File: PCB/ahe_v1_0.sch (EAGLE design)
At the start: 19 parts, among them IC1 MS560702BA03-50, IC2 MCP73871-1CCI_ML, IC3 ESP32-S2-WROOM-I_M22S2H3200UH3, J1 USB3075-30-A

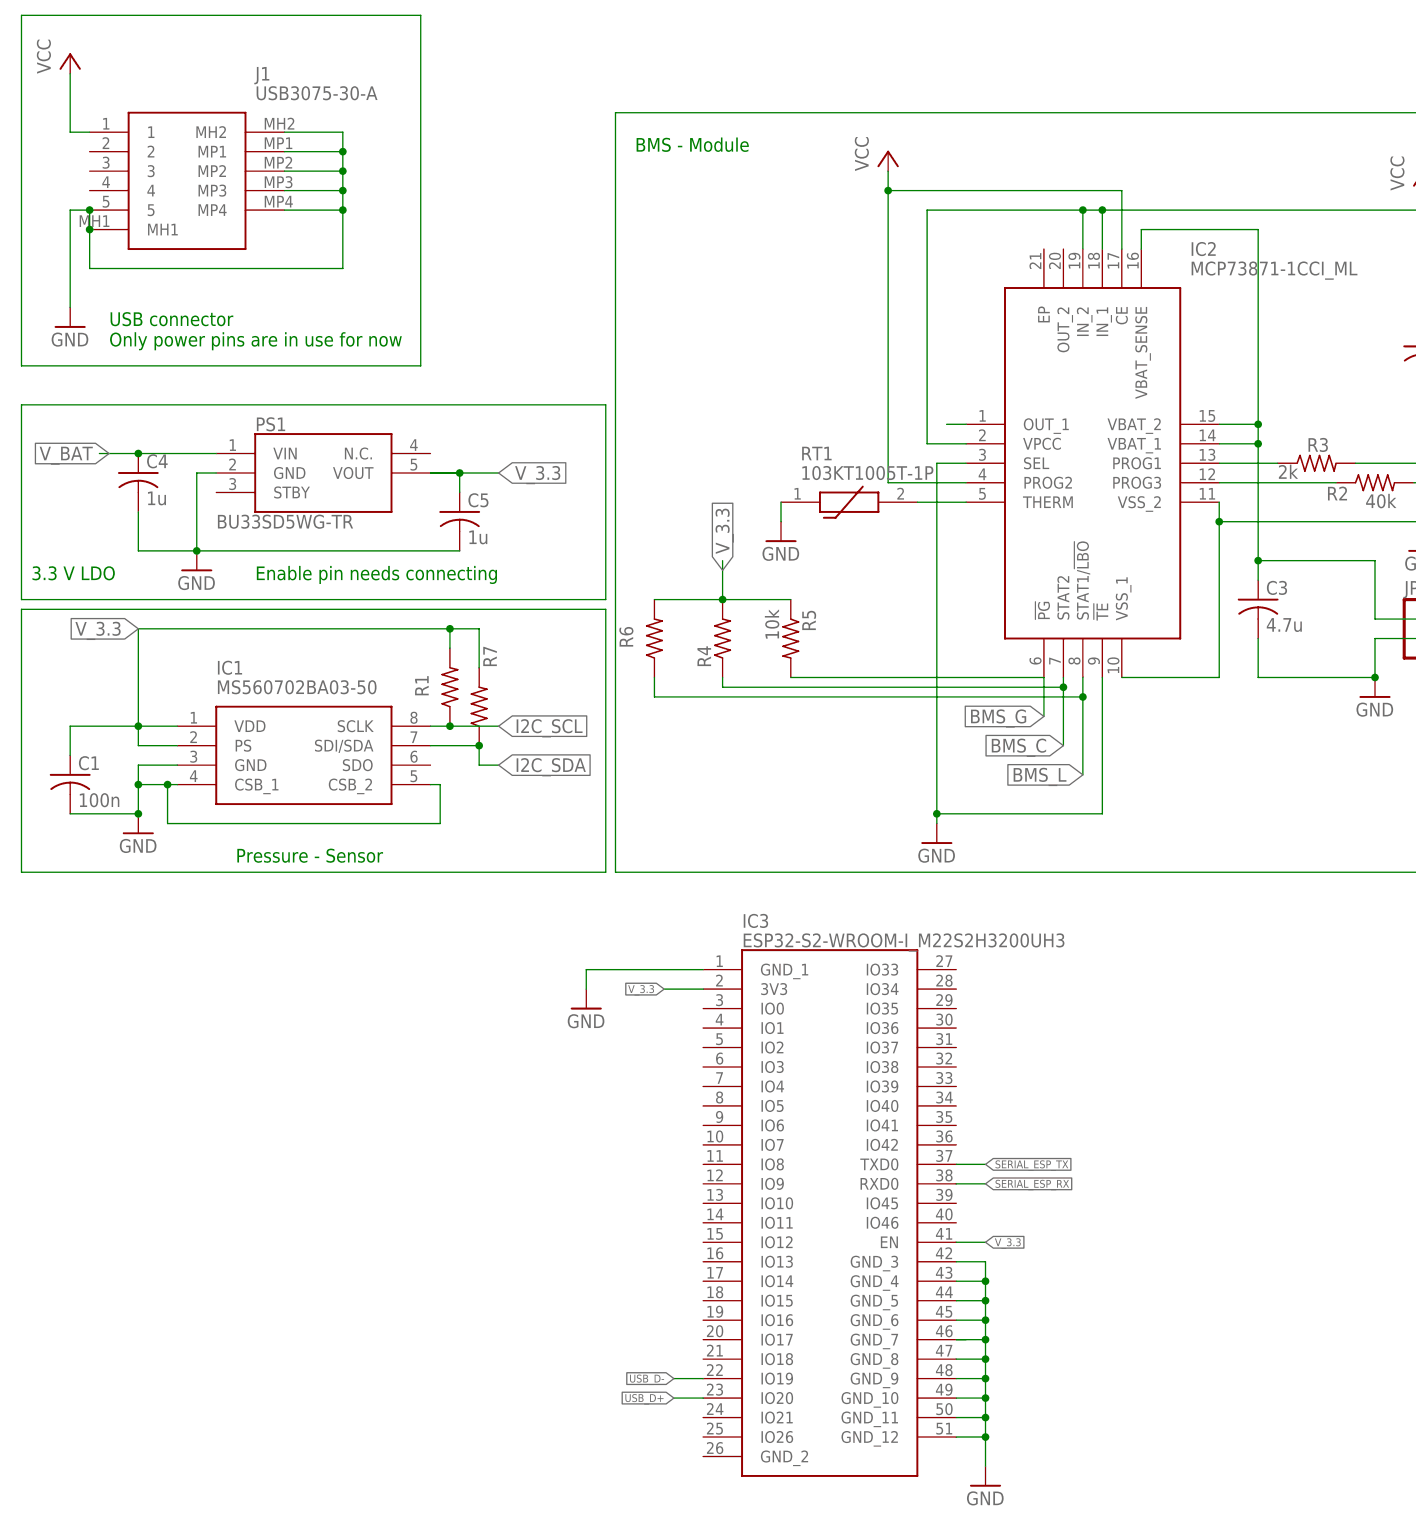
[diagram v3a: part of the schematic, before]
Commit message: #5 #2 added databus and basic IO
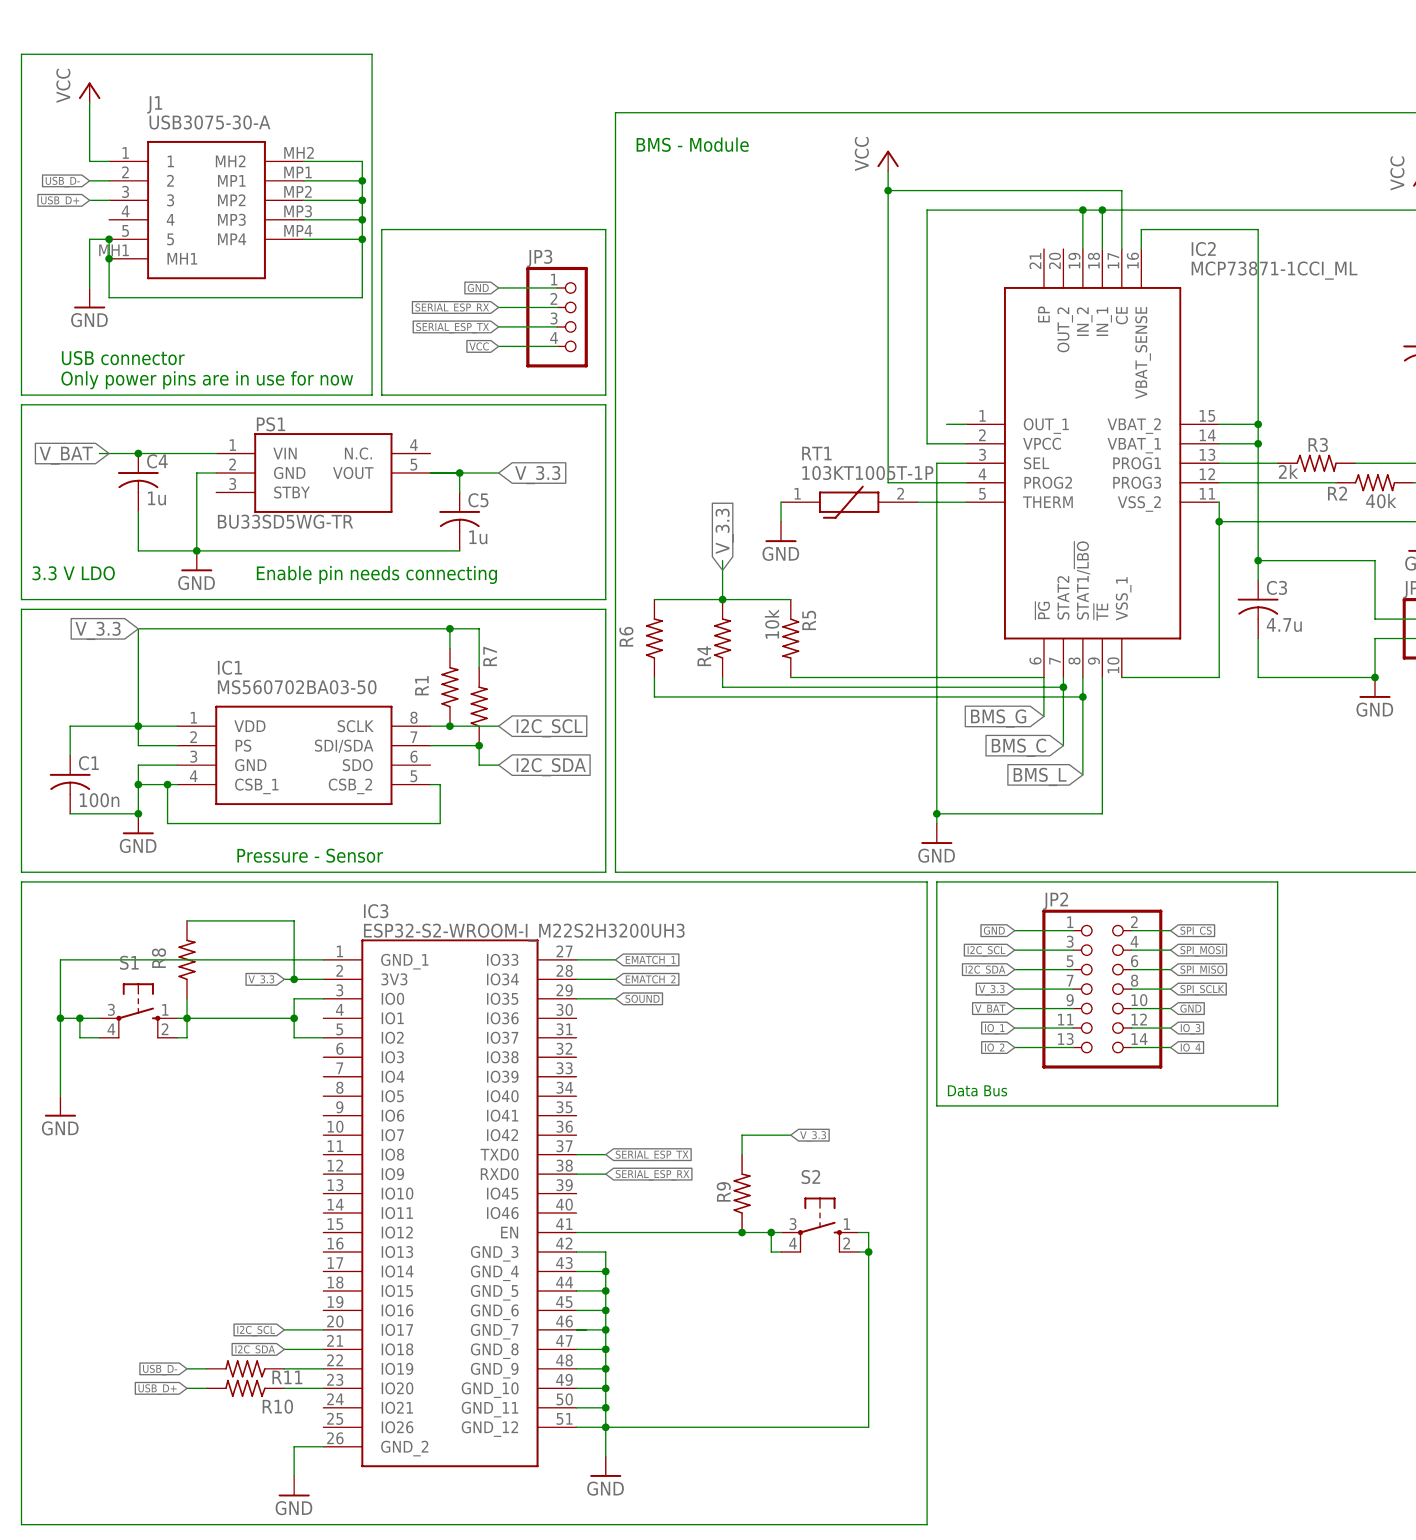
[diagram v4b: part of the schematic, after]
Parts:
- added JP2: (no value), pinhead:PINHD-2X7
- added JP3: (no value), pinhead:PINHD-1X4/90
- added R10, R11: 0, rcl:R-US_R0805
- added R8, R9: 10k, rcl:R-US_R0805
- added S1, S2: (no value), switch-omron:10-XX
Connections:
- new net EMATCH_1: IC3.IO33
- new net EMATCH_2: IC3.IO34
- new net IO_1: JP2.11
- new net IO_2: JP2.13
- new net IO_3: JP2.12
- new net IO_4: JP2.14
- new net N$10: IC3.IO0, IC3.IO2, R8.1, S1.S, S1.S1
- new net N$14: IC3.IO19, R11.1
- new net N$15: IC3.IO20, R10.1
- new net N$9: IC3.EN, R9.1, S2.P, S2.P1
- new net SOUND: IC3.IO35
- new net SPI_CS: JP2.2
- new net SPI_MISO: JP2.6
- new net SPI_MOSI: JP2.4
- new net SPI_SCLK: JP2.8
- net GND: now also IC3.GND_2, JP2.1, JP2.10, JP3.1, S1.P, S1.P1, S2.S, S2.S1
- net I2C_SCL: now also IC3.IO17, JP2.3
- net I2C_SDA: now also IC3.IO18, JP2.5
- net SERIAL_ESP_RX: now also JP3.2
- net SERIAL_ESP_TX: now also JP3.3
- net USB_D+: now also J1.3, R10.2; no longer IC3.IO20
- net USB_D-: now also J1.2, R11.2; no longer IC3.IO19
- net VCC: now also JP3.4
- net V_3.3: now also JP2.7, R8.2, R9.2; no longer IC3.EN
- net V_BAT: now also JP2.9
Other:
- note added: "Data Bus"
- moved on the sheet: IC3, J1

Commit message: full schematic
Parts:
- removed JP1: (no value), pinhead:PINHD-1X2
- added CN1, CN2: 1X4-3.5MM, adafruit:1X4-3.5MM
- added LS1: CMI-9605-0580T, CMI-9605-0580T:CMI-9605-0580T
- added Q1: TSM200N03DPQ33_RGG, TSM200N03DPQ33_RGG:TSM200N03DPQ33_RGG
- added R12: 0, rcl:R-US_R0805
- added R13, R15: 100k, rcl:R-US_R0805
- added R14, R16: 27k, rcl:R-US_R0805
- R10, R11: value 0 -> 33
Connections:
- new net EMATCH_1-: CN1.4, Q1.DRAIN1_1, Q1.DRAIN1_2, Q1.DRAIN1_3, R13.2
- new net EMATCH_2-: CN2.1, Q1.DRAIN2_1, Q1.DRAIN2_2, Q1.DRAIN2_3, R15.2
- new net EMATCH_N+: CN1.3, CN2.2, R12.1
- new net EXT_SW+: CN1.1
- new net EXT_SW-: CN1.2
- new net SENSE_1: IC3.IO3, R13.1, R14.2
- new net SENSE_2: IC3.IO4, R15.1, R16.2
- net EMATCH_1: now also Q1.GATE1
- net EMATCH_2: now also Q1.GATE2
- net GND: now also CN2.4, LS1.-, Q1.SOURCE1, Q1.SOURCE2, R14.1, R16.1; no longer JP1.2
- net SOUND: now also LS1.+
- net V_BAT: now also CN2.3, R12.2; no longer JP1.1

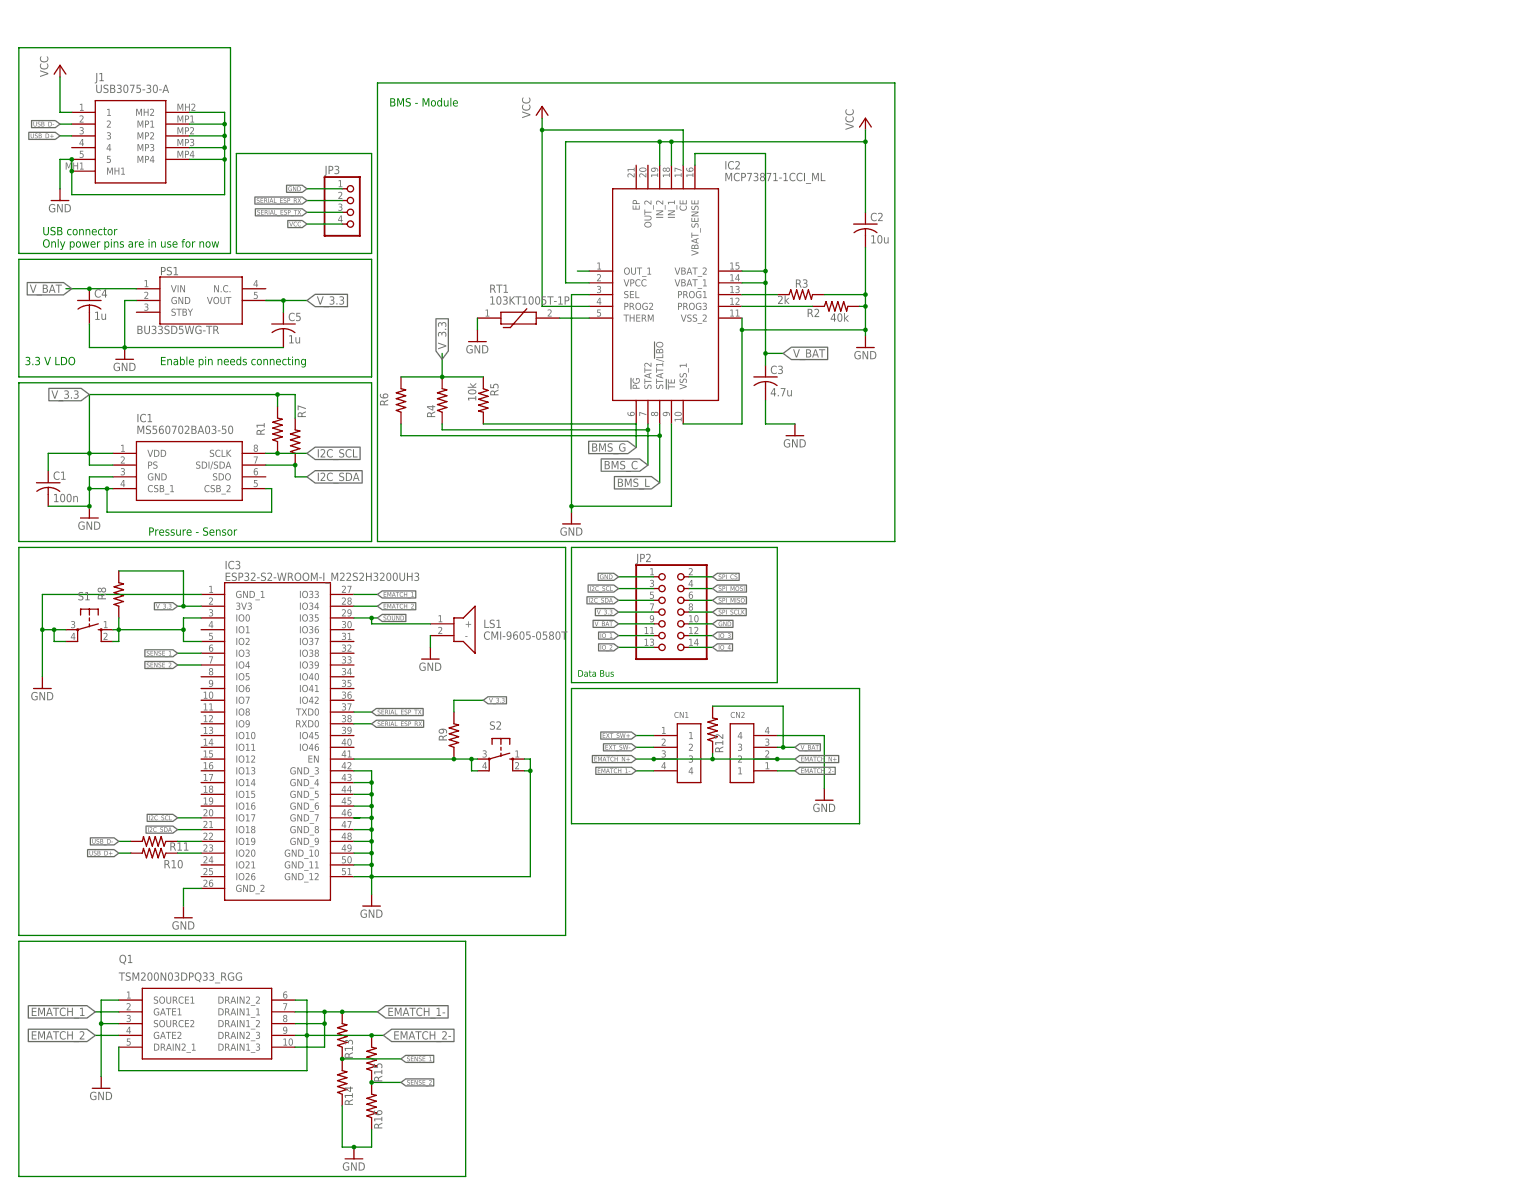
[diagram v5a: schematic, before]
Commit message: #2 board 1 with lipo mounted on the back
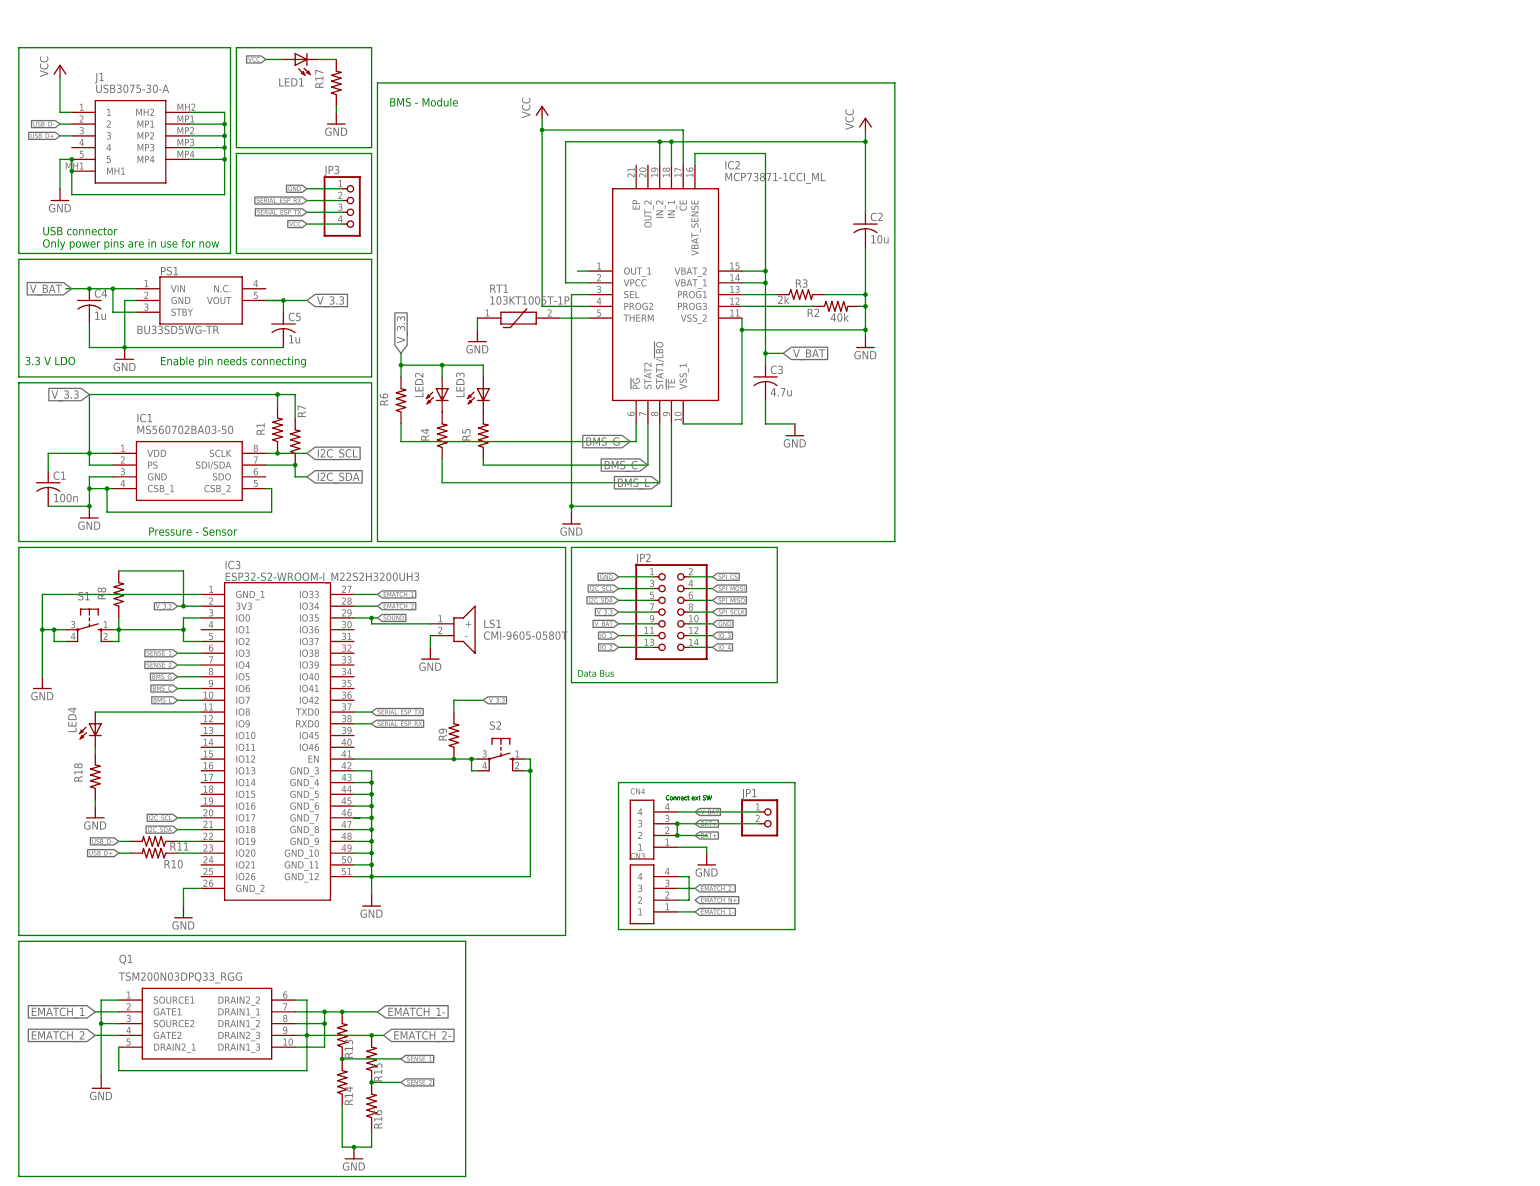
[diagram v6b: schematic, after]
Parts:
- removed CN1, CN2: 1X4-3.5MM, adafruit:1X4-3.5MM
- removed R12: 0, rcl:R-US_R0805
- added CN3, CN4: 1X4-3.5MM, adafruit:1X4-3.5MM
- added JP1: (no value), pinhead:PINHD-1X2
- added LED1, LED2, LED3, LED4: (no value), adafruit:LEDCHIPLED_0805
- added R17, R18: 330, rcl:R-US_R0805
- R4, R5: value 10k -> 330
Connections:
- removed net EXT_SW+: CN1.1
- removed net EXT_SW-: CN1.2
- new net BAT+: CN4.2, CN4.3, JP1.2
- new net N$18: LED1.C, R17.2
- new net N$20: LED2.C, R4.2
- new net N$21: LED3.C, R5.2
- new net N$22: LED4.C, R18.2
- new net N$23: IC3.IO8, LED4.A
- net BMS_C: now also IC3.IO6, R5.1; no longer R4.1
- net BMS_G: now also IC3.IO5, R6.1; no longer R5.2
- net BMS_L: now also IC3.IO7, R4.1; no longer R6.1
- net EMATCH_1-: now also CN3.1; no longer CN1.4
- net EMATCH_2-: now also CN3.3; no longer CN2.1
- net EMATCH_N+: now also CN3.2, CN3.4; no longer CN1.3, CN2.2, R12.1
- net GND: now also CN4.1, R17.1, R18.1; no longer CN2.4
- net VCC: now also LED1.A
- net V_3.3: now also LED2.A, LED3.A; no longer R4.2, R5.1
- net V_BAT: now also CN4.4, JP1.1, PS1.STBY; no longer CN2.3, R12.2
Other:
- note added: "Connect ext SW"
- moved on the sheet: R4, R5
